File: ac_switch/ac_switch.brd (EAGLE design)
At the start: 59.4 x 58.4 mm, 20 parts, among them IC1 TINY85, T1 BC337, X2 SSW-102-02-S-S-RA

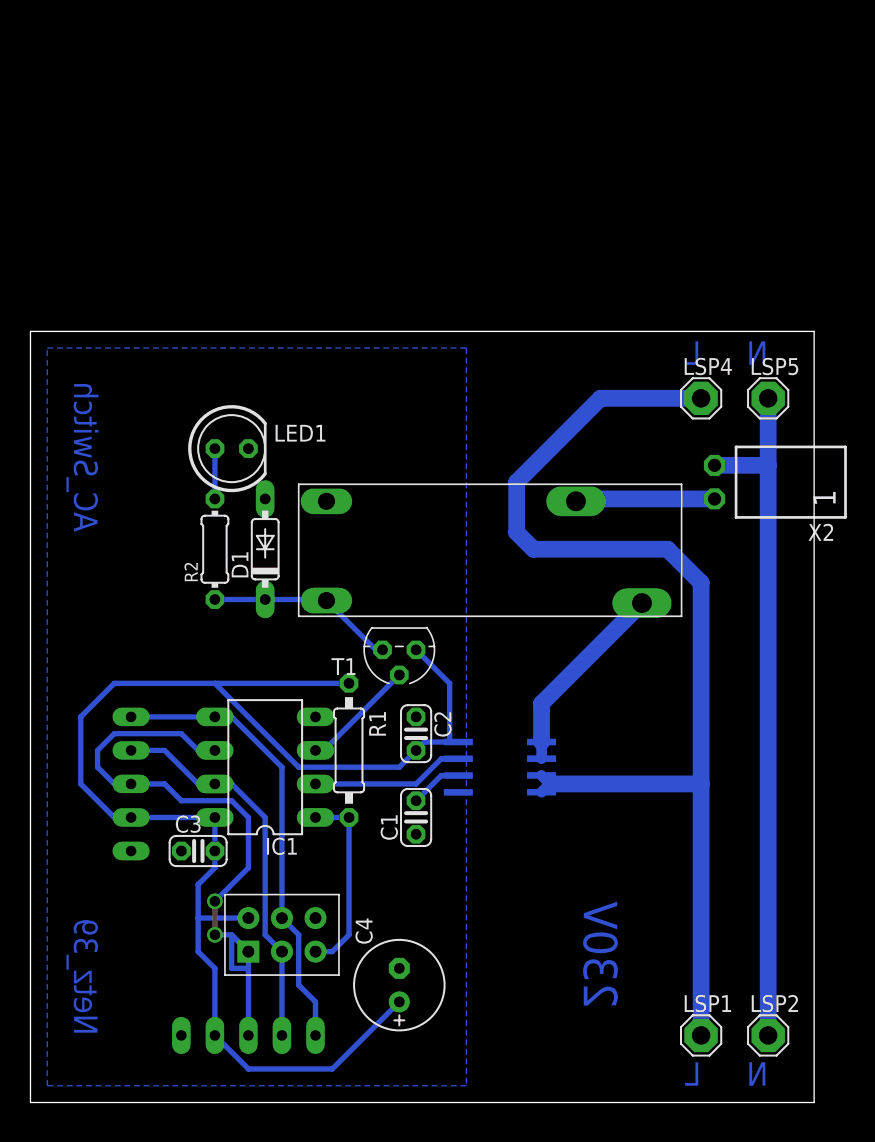
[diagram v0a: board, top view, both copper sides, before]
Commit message: * Transistor in Emitterschaltung (dann mit Vorwiderstand)
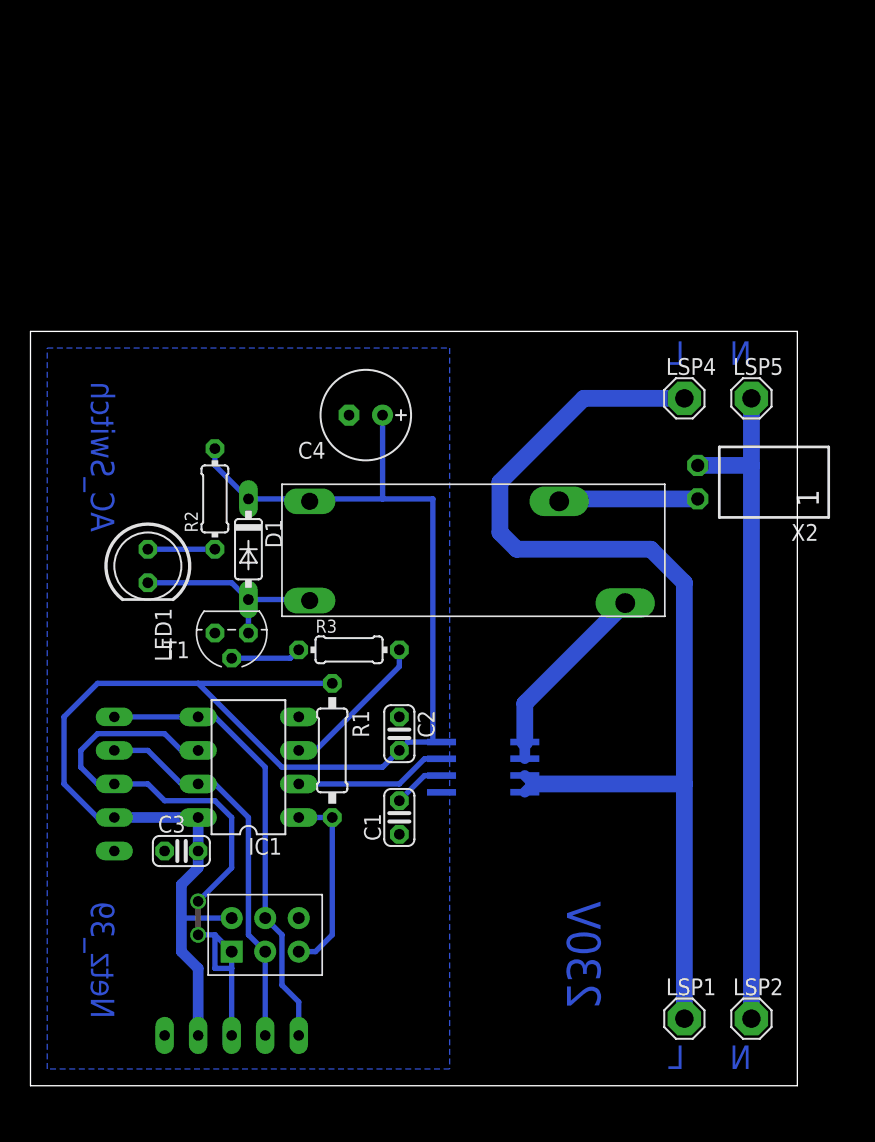
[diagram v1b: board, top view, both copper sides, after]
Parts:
- added R3: 150R, resistor:0204/7
- moved C4 43.3 mm to (25.4, 52.1), turned to 180 degrees
- moved T1 12.8 mm to (15.2, 35.6)
- moved LED1 10.9 mm to (8.89, 40.6), turned to 270 degrees
- moved R2 3.81 mm to (14.0, 45.7)
- moved LSP2 1.80 mm to (54.6, 6.35)
- moved LSP1 1.80 mm to (49.5, 6.35)
- moved LSP5 1.27 mm to (54.6, 53.3)
- moved U$2 1.27 mm to (34.3, 25.4)
- moved X2 1.27 mm to (52.1, 47.0)
- moved U$5 1.27 mm to (15.2, 5.08)
- moved U$3 1.27 mm to (6.35, 24.1)
- moved C1 1.27 mm to (27.9, 21.6)
- moved C2 1.27 mm to (27.9, 27.9)
- moved C3 1.27 mm to (11.4, 19.1)
- moved D1 1.27 mm to (16.5, 41.9), turned to 270 degrees
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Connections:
- new net N$4: LED1.A, R2.1
- net GND: now also T1.1; no longer D1.A, LED1.K, U$1.P$2
- net N$1: now also D1.A, LED1.K, T1.3; no longer D1.C, R2.1, T1.1
- net N$5: now also R3.1, T1.2; no longer LED1.A, R2.2
- net SWITCH: now also R3.2; no longer T1.2
- net VCC: now also D1.C, R2.2, U$1.P$2; no longer T1.3
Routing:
- net VCC: track 106.1 -> 124.6 mm
- net N$4: track 0.00 -> 5.08 mm
- net SWITCH: track 8.72 -> 11.5 mm
- net N$5: track 3.81 -> 5.34 mm
- net L: track 83.5 -> 82.2 mm
- net N: track 52.3 -> 51.1 mm
- net N$1: track 14.3 -> 15.4 mm
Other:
- board size 59.4 x 58.4 mm -> 58.1 x 57.1 mm

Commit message: * Werte für Widerstände und Kondensator (inkl. Package) angepasst * fine-tuning am PCB-Layout
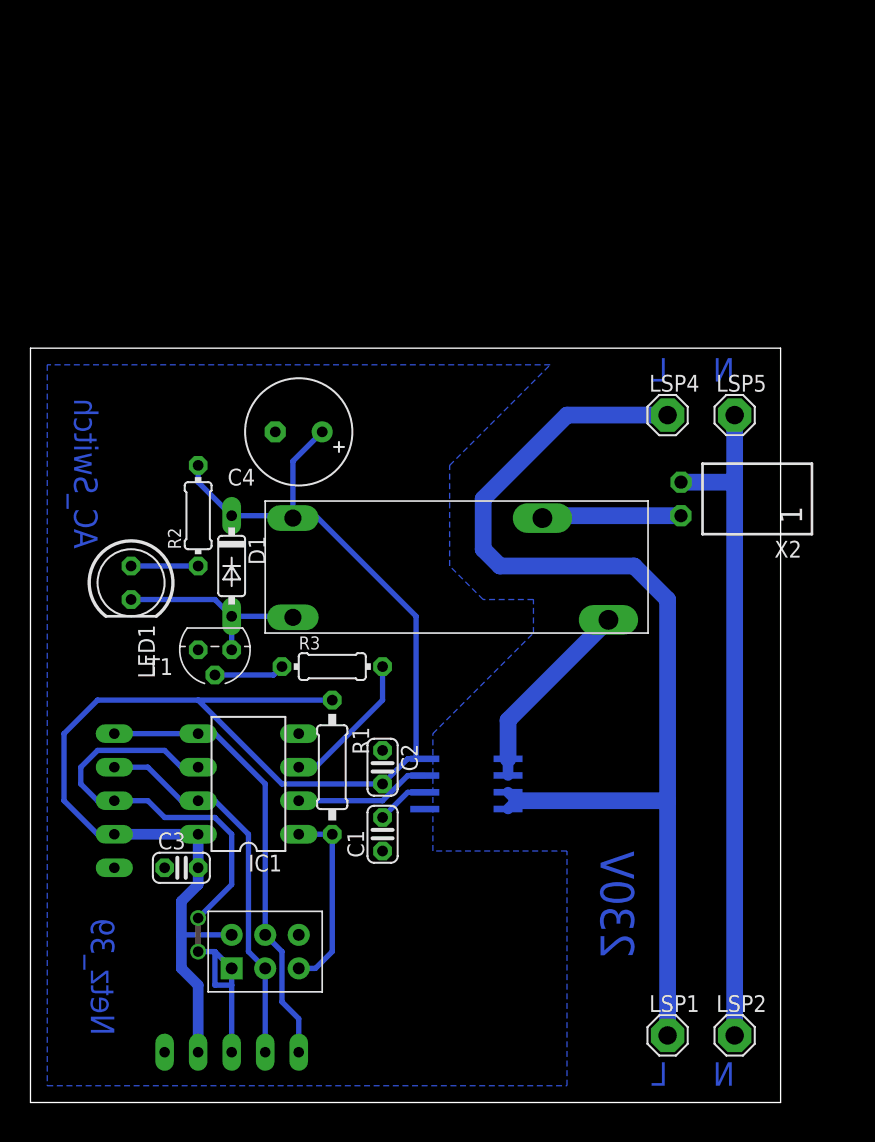
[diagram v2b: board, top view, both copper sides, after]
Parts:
- C4: value 470µ -> 68µ; device resistor:E2,5-7 -> resistor:E3,5-8
- R2: value 150R -> 220R
- R3: value 150R -> 1,5K
- moved C4 5.24 mm to (20.3, 50.8)
- moved C2 2.84 mm to (26.7, 25.4)
- moved LSP4 1.80 mm to (48.3, 52.1)
- moved X2 1.80 mm to (50.8, 45.7)
- moved LED1 1.80 mm to (7.62, 39.4)
- moved LSP1 1.80 mm to (48.3, 5.08)
- moved T1 1.80 mm to (14.0, 34.3)
- moved C1 1.80 mm to (26.7, 20.3)
- moved LSP5 1.80 mm to (53.3, 52.1)
- moved D1 1.80 mm to (15.2, 40.6)
- moved R2 1.80 mm to (12.7, 44.5)
- moved LSP2 1.80 mm to (53.3, 5.08)
- moved R3 1.80 mm to (22.9, 33.0)
- moved U$1 1.80 mm to (17.8, 35.6)
- moved U$2 1.80 mm to (33.0, 24.1)
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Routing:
- net VCC: track 124.6 -> 120.0 mm
- net SENSE: track 11.6 -> 10.3 mm
- net SWITCH: track 11.5 -> 11.0 mm
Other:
- board size 58.1 x 57.1 mm -> 56.8 x 57.1 mm

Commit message: Overlap behoben
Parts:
- moved C2 2.84 mm to (27.9, 27.9), turned to 0 degrees
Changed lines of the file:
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@@
 <element name="T1" library="transistor" package="TO92" value="BC337" x="13.97" y="34.29" rot="R180"/>
 <element name="C1" library="resistor" package="C025-024X044" value="1n" x="26.67" y="20.32" rot="R90"/>
-<element name="C2" library="resistor" package="C025-024X044" value="100n" x="26.67" y="25.4" rot="R270"/>
+<element name="C2" library="resistor" package="C025-024X044" value="100n" x="27.94" y="27.94"/>
 <element name="IC1" library="atmel" package="DIL08" value="TINY85" x="16.51" y="24.13" rot="R90">
 <attribute name="OC_NEWARK" value="unknown" x="22.86" y="59.69" size="1.778" layer="27" rot="R90" display="off"/>
@@
 <wire x1="22.098" y1="50.8" x2="19.88" y2="48.582" width="0.4064" layer="16"/>
 <wire x1="19.88" y1="48.582" x2="19.88" y2="44.27" width="0.4064" layer="16"/>
-<wire x1="26.67" y1="24.13" x2="19.05" y2="24.13" width="0.4064" layer="16"/>
-<wire x1="26.67" y1="24.13" x2="28.575" y2="26.035" width="0.4064" layer="16"/>
 <wire x1="19.88" y1="44.27" x2="20.06" y2="44.45" width="0.4064" layer="16"/>
 <wire x1="20.06" y1="44.45" x2="21.59" y2="44.45" width="0.4064" layer="16"/>
 <wire x1="21.59" y1="44.45" x2="29.21" y2="36.83" width="0.4064" layer="16"/>
-<wire x1="29.21" y1="36.83" x2="29.21" y2="26.035" width="0.4064" layer="16"/>
+<wire x1="29.21" y1="36.83" x2="29.21" y2="27.94" width="0.4064" layer="16"/>
+<wire x1="29.21" y1="26.67" x2="29.21" y2="26.035" width="0.4064" layer="16"/>
+<wire x1="28.575" y1="26.035" x2="26.67" y2="24.13" width="0.4064" layer="16"/>
+<wire x1="26.67" y1="24.13" x2="19.05" y2="24.13" width="0.4064" layer="16"/>
+<wire x1="29.21" y1="27.94" x2="29.21" y2="26.67" width="0.4064" layer="16"/>
 </signal>
 <signal name="N$1">

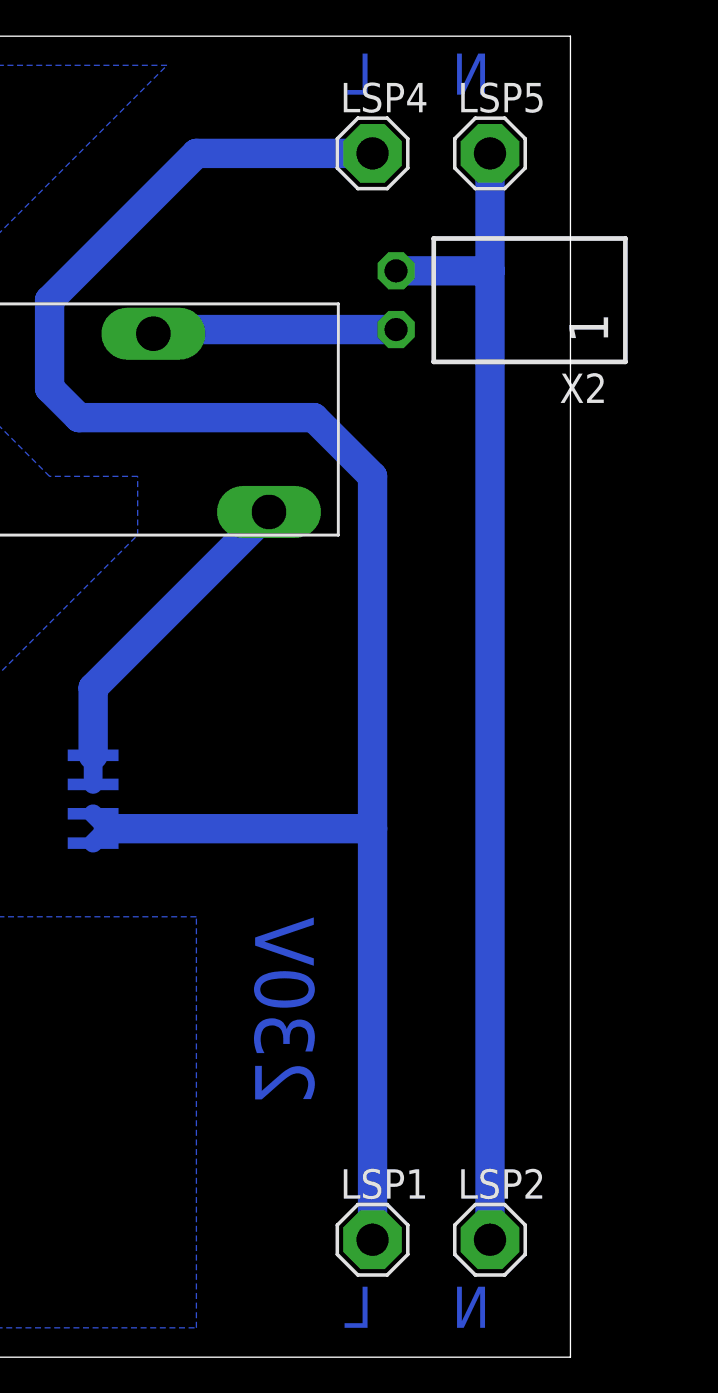
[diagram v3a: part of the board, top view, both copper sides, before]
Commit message: Jetzt auch mit den richtigen Anschlussklemmen
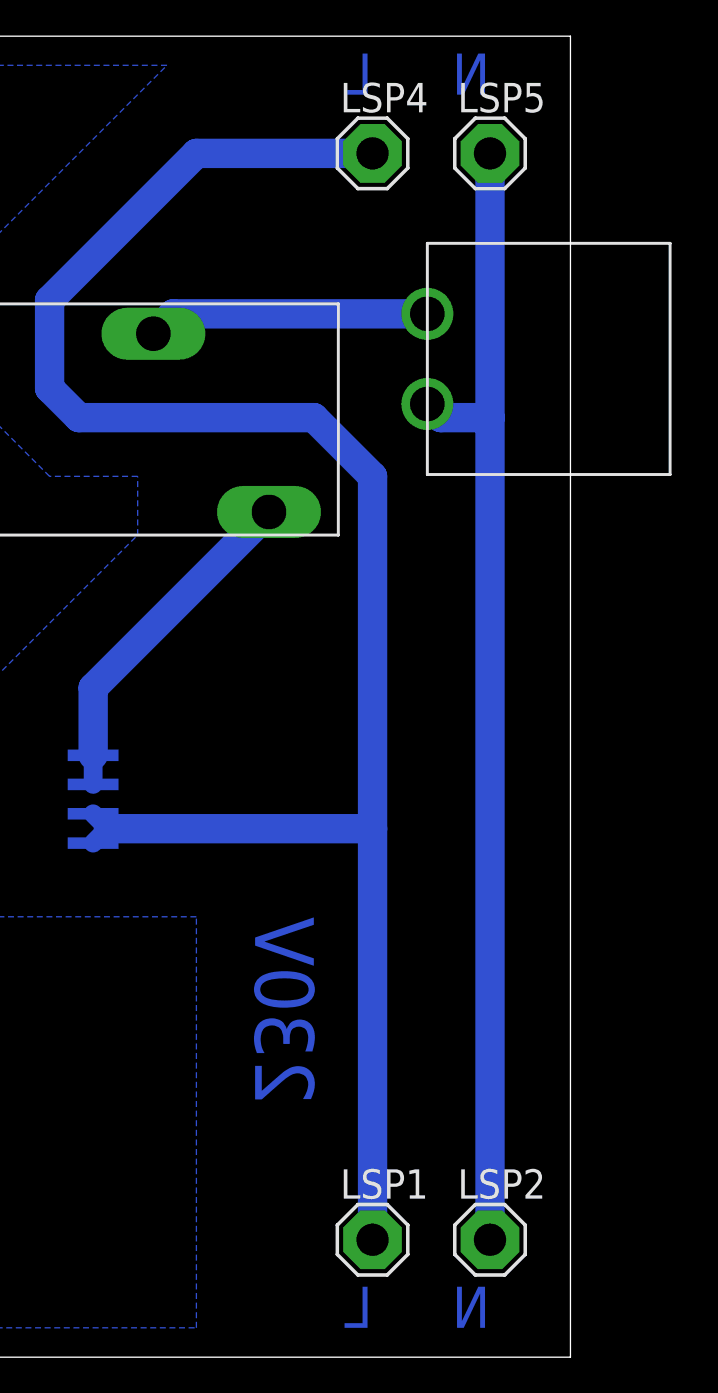
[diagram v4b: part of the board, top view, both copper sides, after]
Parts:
- removed X2: SSW-102-02-S-S-RA, con-samtec:SSW-102-02-S-S-RA
- added U$6: WAGO_734_262, n39:WAGO_734_262
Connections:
- net L_OUT: now also U$6.P$1; no longer X2.1
- net N: now also U$6.P$2; no longer X2.2
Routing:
- net L_OUT: track 10.6 -> 12.2 mm
- net N: track 51.1 -> 49.9 mm
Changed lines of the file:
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@@
 <element name="C4" library="resistor" package="E3,5-8" value="68µ" x="20.32" y="50.8" rot="R180"/>
 <element name="U$5" library="n39" package="I3C_PADS" value="I3C_PORT" x="15.24" y="3.81" rot="R90"/>
-<element name="X2" library="con-samtec" package="SSW-102-02-S-S-RA" value="SSW-102-02-S-S-RA" x="50.8" y="45.72" rot="R90">
-<attribute name="OC_NEWARK" value="11P9352" x="50.8" y="45.72" size="1.778" layer="27" rot="R90" display="off"/>
-<attribute name="MPN" value="SSW-102-02-S-S-RA" x="50.8" y="45.72" size="1.778" layer="27" rot="R90" display="off"/>
-<attribute name="MF" value="" x="50.8" y="45.72" size="1.778" layer="27" rot="R90" display="off"/>
-<attribute name="OC_FARNELL" value="unknown" x="50.8" y="45.72" size="1.778" layer="27" rot="R90" display="off"/>
-</element>
 <element name="R3" library="resistor" package="0204/7" value="1,5K" x="22.86" y="33.02"/>
+<element name="U$6" library="n39" package="WAGO_734_262" value="WAGO_734_262" x="55.88" y="43.18" rot="R270"/>
 </elements>
 <signals>
@@
 <contactref element="LSP2" pad="MP"/>
 <contactref element="LSP5" pad="MP"/>
-<wire x1="53.34" y1="52.07" x2="53.34" y2="46.99" width="1.27" layer="16"/>
-<wire x1="53.34" y1="46.99" x2="53.34" y2="5.08" width="1.27" layer="16"/>
-<contactref element="X2" pad="2"/>
-<wire x1="49.276" y1="46.99" x2="53.34" y2="46.99" width="1.27" layer="16"/>
+<wire x1="53.34" y1="52.07" x2="53.34" y2="40.64" width="1.27" layer="16"/>
+<contactref element="U$6" pad="P$2"/>
+<wire x1="53.34" y1="40.64" x2="53.34" y2="5.08" width="1.27" layer="16"/>
+<wire x1="50.63" y1="41.23" x2="51.22" y2="40.64" width="1.27" layer="16"/>
+<wire x1="51.22" y1="40.64" x2="53.34" y2="40.64" width="1.27" layer="16"/>
 </signal>
 <signal name="N$3">
@@
 <signal name="L_OUT">
 <contactref element="U$1" pad="P$3"/>
-<contactref element="X2" pad="1"/>
-<wire x1="49.276" y1="44.45" x2="39.37" y2="44.45" width="1.27" layer="16"/>
-<wire x1="39.37" y1="44.45" x2="39.19" y2="44.27" width="1.27" layer="16"/>
-<wire x1="39.19" y1="44.27" x2="38.78" y2="44.27" width="1.27" layer="16"/>
+<contactref element="U$6" pad="P$1"/>
+<wire x1="38.78" y1="44.27" x2="39.64" y2="45.13" width="1.27" layer="16"/>
+<wire x1="39.64" y1="45.13" x2="50.63" y2="45.13" width="1.27" layer="16"/>
 </signal>
 <signal name="N$4">

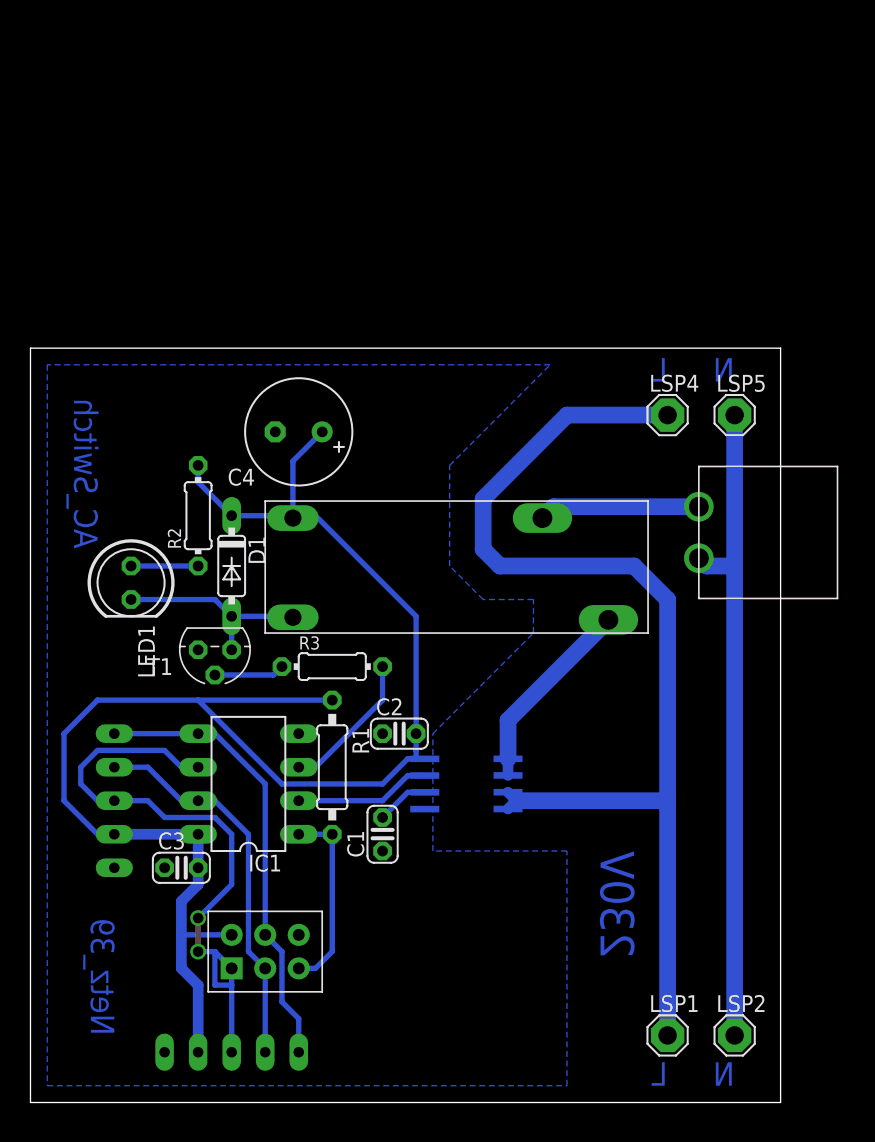
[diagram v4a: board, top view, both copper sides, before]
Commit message: Platinenlayout angepasst, sodass es zum Power-Board passt
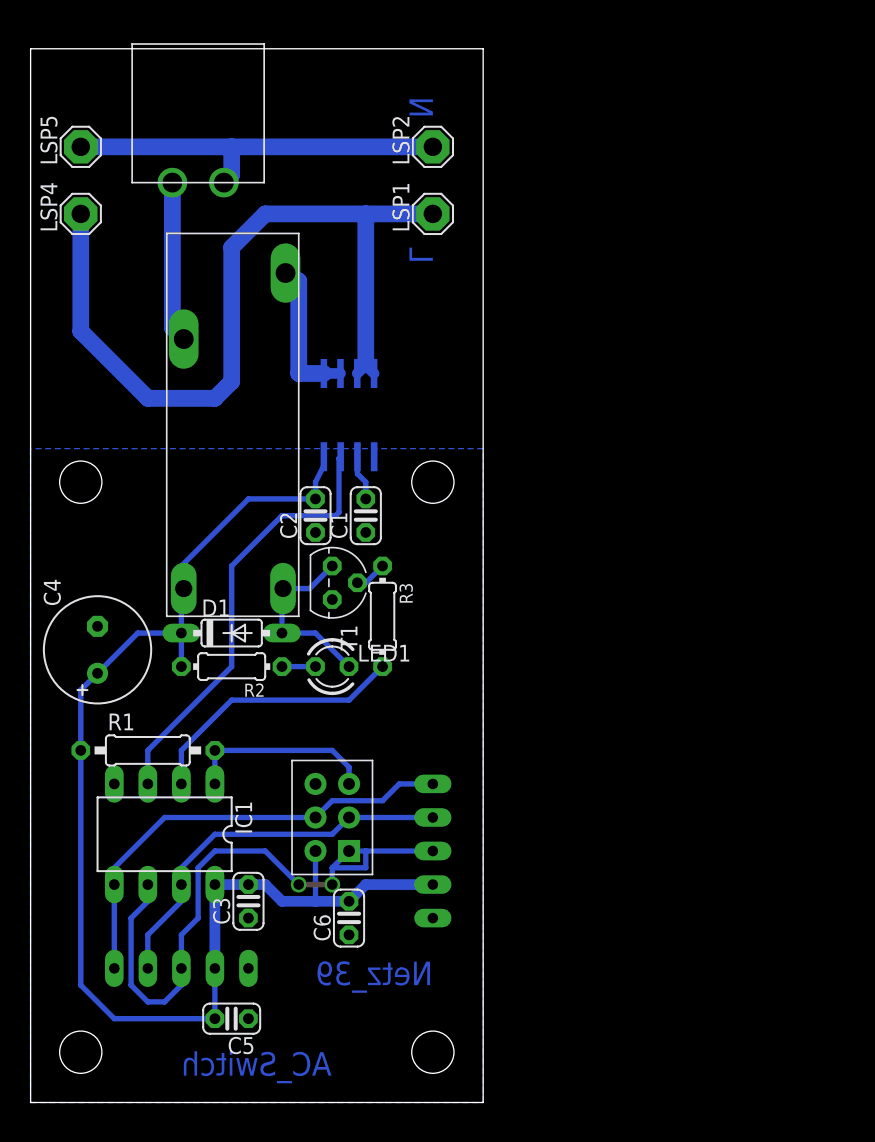
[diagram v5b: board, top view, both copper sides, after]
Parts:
- added C5, C6: 100n, resistor:C025-024X044
- LED1: device led:LED5MM -> led:LED3MM
- moved LSP2 71.1 mm to (30.5, 72.4), turned to 90 degrees
- moved LSP1 64.7 mm to (30.5, 67.3), turned to 90 degrees
- moved U$6 53.6 mm to (12.7, 74.9), turned to 0 degrees
- moved LSP5 53.5 mm to (3.81, 72.4), turned to 90 degrees
- moved LSP4 47.0 mm to (3.81, 67.3), turned to 90 degrees
- moved U$2 29.3 mm to (24.1, 52.1), turned to 180 degrees
- moved C1 24.2 mm to (25.4, 44.5)
- moved C4 22.5 mm to (5.08, 34.3), turned to 90 degrees
- moved U$5 21.6 mm to (30.5, 19.1), turned to 180 degrees
- moved C2 17.7 mm to (21.6, 44.5), turned to 90 degrees
- moved LED1 16.5 mm to (22.9, 33.0), turned to 0 degrees
- moved R1 14.0 mm to (8.89, 26.7), turned to 0 degrees
- moved U$3 13.7 mm to (11.4, 10.2), turned to 270 degrees
- moved R2 11.7 mm to (15.2, 33.0), turned to 180 degrees
- moved U$4 11.4 mm to (22.9, 21.6), turned to 180 degrees
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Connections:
- net GND: now also C5.1, C6.1
- net SENSE: now also IC1.3; no longer IC1.2
- net SWITCH: now also IC1.2; no longer IC1.3
- net VCC: now also C5.2, C6.2
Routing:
- net SENSE: track 10.3 -> 33.2 mm
- net VCC: track 120.0 -> 97.9 mm
- net N: track 49.9 -> 29.6 mm
- net L: track 82.2 -> 62.7 mm
- net SWITCH: track 11.0 -> 20.4 mm
- net N$3: track 15.0 -> 11.4 mm
- net N$5: track 5.34 -> 2.43 mm
- net N$4: track 5.08 -> 2.54 mm
- net N$1: track 15.4 -> 14.0 mm
- net N$2: track 3.99 -> 3.46 mm
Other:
- board size 56.8 x 57.1 mm -> 34.3 x 79.8 mm
- board text removed: "230V"
